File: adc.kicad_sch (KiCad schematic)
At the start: 0 parts

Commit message: First schematic version of AF
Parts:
- added U6: LTC2299xUP, Package_DFN_QFN:QFN-64-1EP_9x9mm_P0.5mm_EP7.15x7.15mm, symbol Analog_ADC:LTC2299xUP
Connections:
- new net: U6.11 (REFLB), U6.12 (REFLB)
- new net: U6.13 (REFHB), U6.14 (REFHB)
- new net: U6.17 (GND), U6.64 (GND), U6.65 (GND)
- new net: U6.3 (REFHA), U6.4 (REFHA)
- new net: U6.31 (OGND), U6.50 (OGND)
- new net: U6.5 (REFLA), U6.6 (REFLA)
- new net CH1_CH+: U6.1 (AINA+)
- new net CH1_CH-: U6.2 (AINA-)
- new net CH1_COMMON: U6.61 (VCMA)
- new net CH2_CH+: U6.16 (AINB+)
- new net CH2_CH-: U6.15 (AINB-)
- new net CH2_COMMON: U6.20 (VCMB)

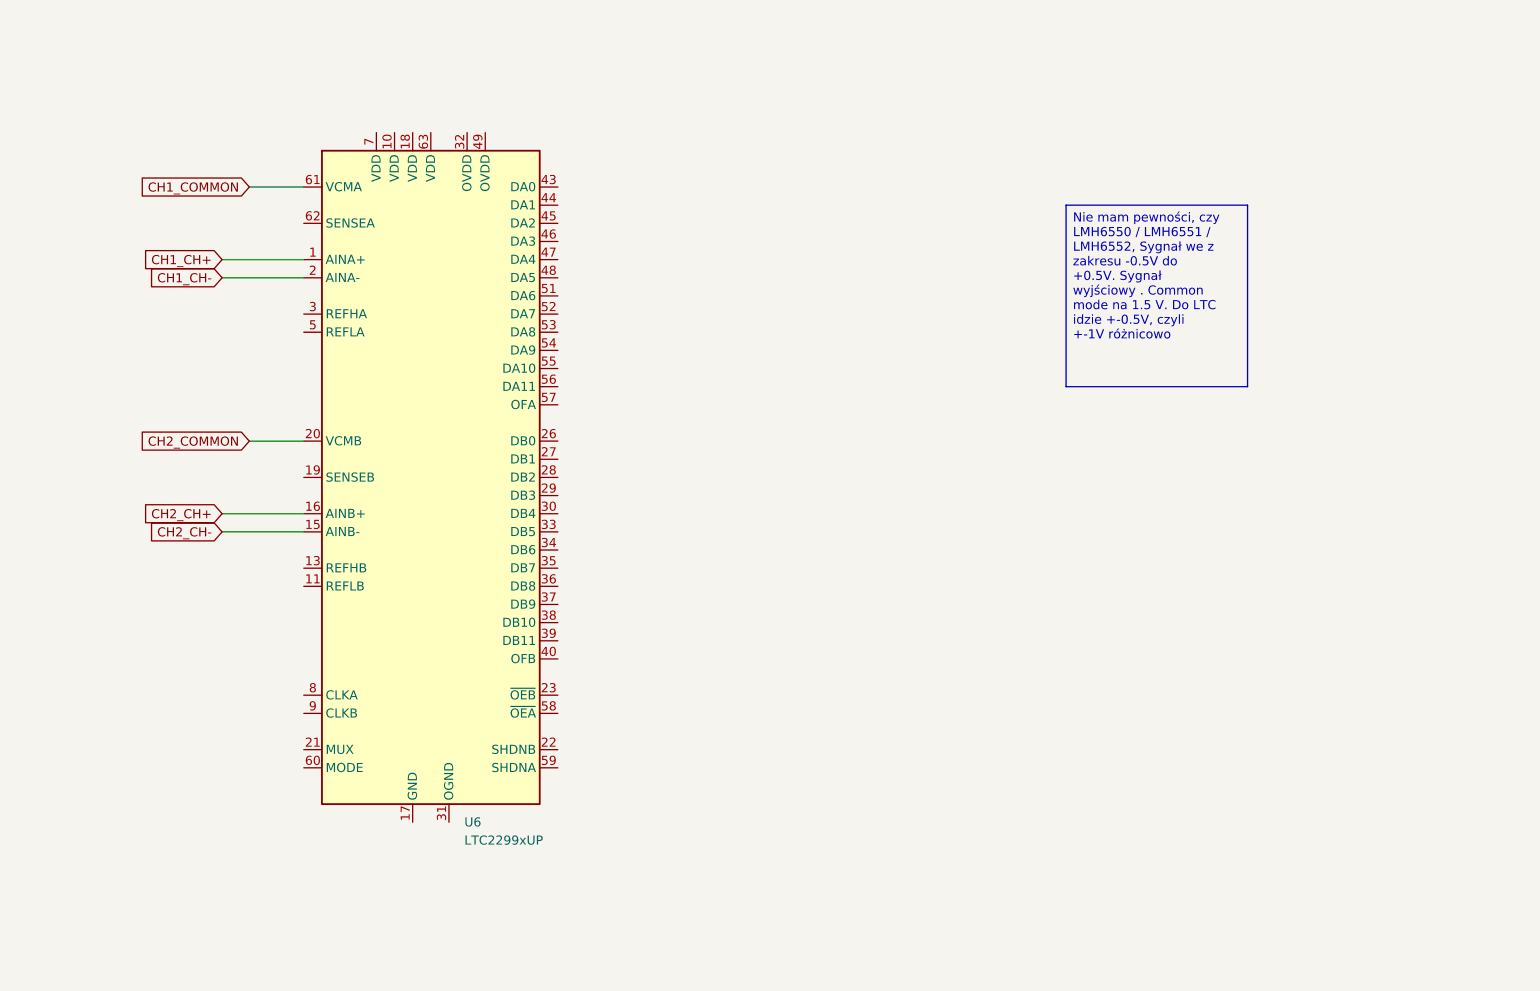
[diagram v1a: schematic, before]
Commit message: Chose amplifiers
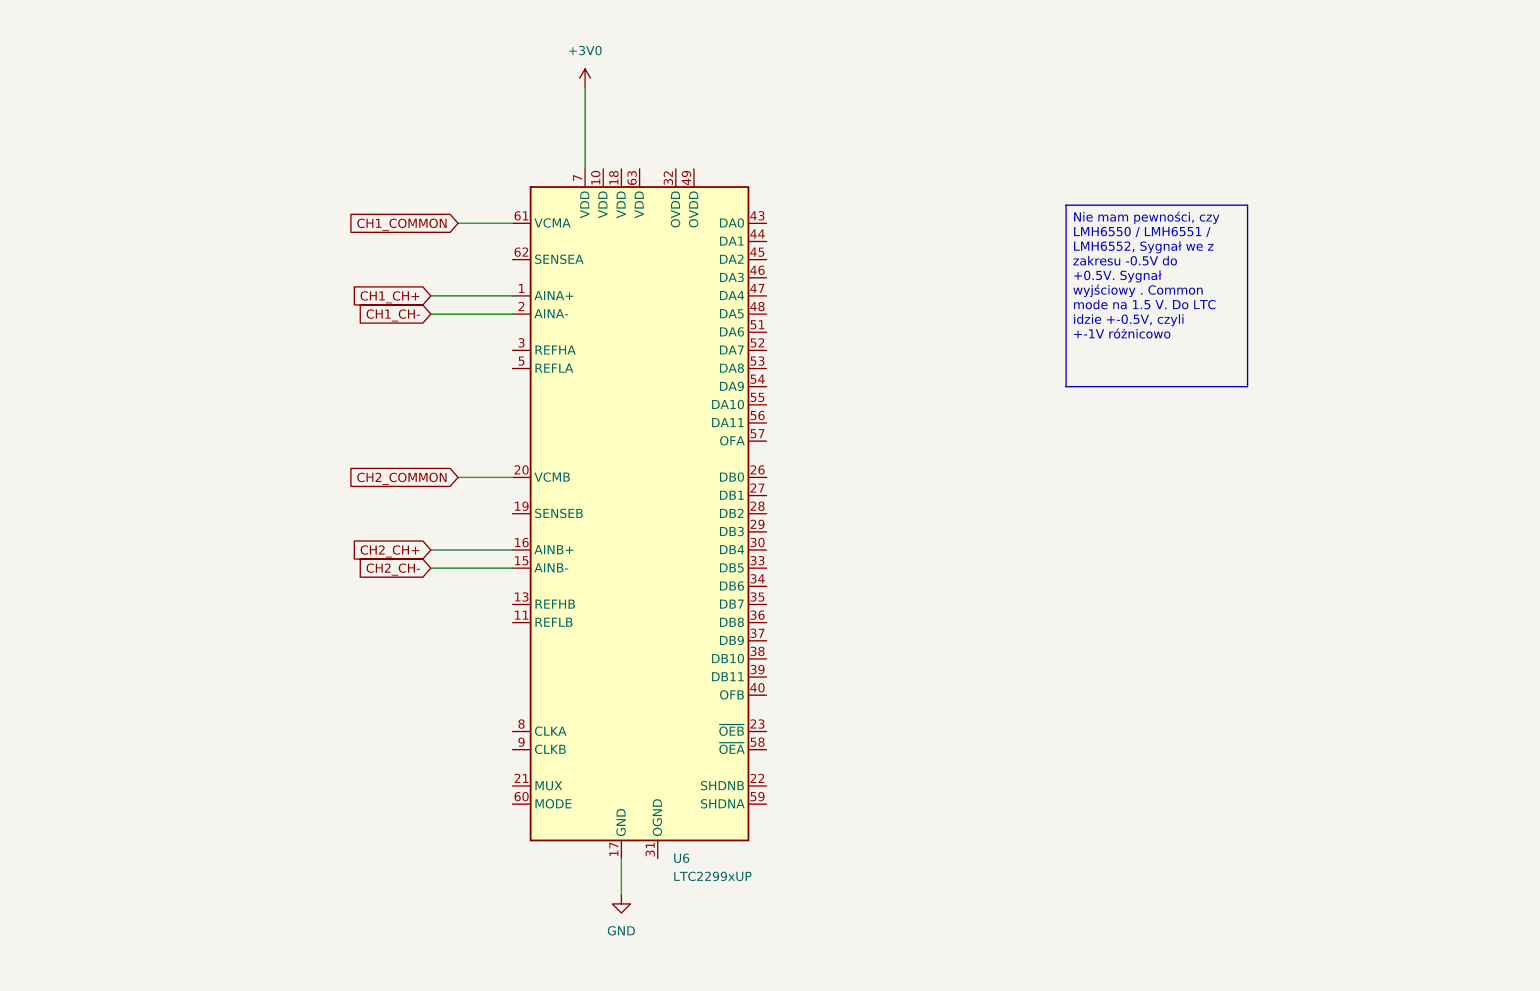
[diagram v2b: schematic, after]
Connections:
- net GND: now reaches U6.17 (GND), U6.64 (GND), U6.65 (GND)
- net +3V0: now reaches U6.7 (VDD)
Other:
- moved on the sheet: U6
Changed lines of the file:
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@@
 	(wire
 		(pts
-			(xy 92.71 91.44) (xy 104.14 91.44)
-		)
-		(stroke
-			(width 0)
-			(type default)
-		)
-	)
-	(wire
-		(pts
-			(xy 96.52 45.72) (xy 104.14 45.72)
-		)
-		(stroke
-			(width 0)
-			(type default)
-		)
-	)
-	(wire
-		(pts
-			(xy 92.71 55.88) (xy 104.14 55.88)
-		)
-		(stroke
-			(width 0)
-			(type default)
-		)
-	)
-	(wire
-		(pts
-			(xy 92.71 58.42) (xy 104.14 58.42)
-		)
-		(stroke
-			(width 0)
-			(type default)
-		)
-	)
-	(wire
-		(pts
-			(xy 96.52 81.28) (xy 104.14 81.28)
-		)
-		(stroke
-			(width 0)
-			(type default)
-		)
-	)
-	(wire
-		(pts
-			(xy 92.71 93.98) (xy 104.14 93.98)
+			(xy 143.51 31.75) (xy 143.51 43.18)
+		)
+		(stroke
+			(width 0)
+			(type default)
+		)
+	)
+	(wire
+		(pts
+			(xy 121.92 96.52) (xy 133.35 96.52)
+		)
+		(stroke
+			(width 0)
+			(type default)
+		)
+	)
+	(wire
+		(pts
+			(xy 125.73 50.8) (xy 133.35 50.8)
+		)
+		(stroke
+			(width 0)
+			(type default)
+		)
+	)
+	(wire
+		(pts
+			(xy 121.92 60.96) (xy 133.35 60.96)
+		)
+		(stroke
+			(width 0)
+			(type default)
+		)
+	)
+	(wire
+		(pts
+			(xy 121.92 63.5) (xy 133.35 63.5)
+		)
+		(stroke
+			(width 0)
+			(type default)
+		)
+	)
+	(wire
+		(pts
+			(xy 125.73 86.36) (xy 133.35 86.36)
+		)
+		(stroke
+			(width 0)
+			(type default)
+		)
+	)
+	(wire
+		(pts
+			(xy 148.59 139.7) (xy 148.59 144.78)
+		)
+		(stroke
+			(width 0)
+			(type default)
+		)
+	)
+	(wire
+		(pts
+			(xy 121.92 99.06) (xy 133.35 99.06)
 		)
 		(stroke
@@
 	(global_label "CH2_CH-"
 		(shape input)
-		(at 92.71 93.98 180)
+		(at 121.92 99.06 180)
 		(fields_autoplaced yes)
 		(effects
@@
 		)
 		(property "Intersheetrefs" "${INTERSHEET_REFS}"
-			(at 80.7743 93.98 0)
+			(at 109.9843 99.06 0)
 			(effects
 				(font
@@
 	(global_label "CH1_CH+"
 		(shape input)
-		(at 92.71 55.88 180)
+		(at 121.92 60.96 180)
 		(fields_autoplaced yes)
 		(effects
@@
 		)
 		(property "Intersheetrefs" "${INTERSHEET_REFS}"
-			(at 80.7743 55.88 0)
+			(at 109.9843 60.96 0)
 			(effects
 				(font
@@
 	(global_label "CH1_CH-"
 		(shape input)
-		(at 92.71 58.42 180)
+		(at 121.92 63.5 180)
 		(fields_autoplaced yes)
 		(effects
@@
 		)
 		(property "Intersheetrefs" "${INTERSHEET_REFS}"
-			(at 80.7743 58.42 0)
+			(at 109.9843 63.5 0)
 			(effects
 				(font
@@
 	(global_label "CH1_COMMON"
 		(shape input)
-		(at 96.52 45.72 180)
+		(at 125.73 50.8 180)
 		(fields_autoplaced yes)
 		(effects
@@
 		)
 		(property "Intersheetrefs" "${INTERSHEET_REFS}"
-			(at 80.5929 45.72 0)
+			(at 109.8029 50.8 0)
 			(effects
 				(font
@@
 	(global_label "CH2_COMMON"
 		(shape input)
-		(at 96.52 81.28 180)
+		(at 125.73 86.36 180)
 		(fields_autoplaced yes)
 		(effects
@@
 		)
 		(property "Intersheetrefs" "${INTERSHEET_REFS}"
-			(at 80.5929 81.28 0)
+			(at 109.8029 86.36 0)
 			(effects
 				(font
@@
 	(global_label "CH2_CH+"
 		(shape input)
-		(at 92.71 91.44 180)
+		(at 121.92 96.52 180)
 		(fields_autoplaced yes)
 		(effects
@@
 		)
 		(property "Intersheetrefs" "${INTERSHEET_REFS}"
-			(at 80.7743 91.44 0)
+			(at 109.9843 96.52 0)
 			(effects
 				(font
@@
 	(symbol
 		(lib_id "Analog_ADC:LTC2299xUP")
-		(at 121.92 86.36 0)
+		(at 151.13 91.44 0)
 		(unit 1)
 		(exclude_from_sim no)
@@
 		(fields_autoplaced yes)
 		(property "Reference" "U6"
-			(at 126.6033 134.62 0)
+			(at 155.8133 139.7 0)
 			(effects
 				(font
@@
 		)
 		(property "Value" "LTC2299xUP"
-			(at 126.6033 137.16 0)
+			(at 155.8133 142.24 0)
 			(effects
 				(font
@@
 		)
 		(property "Footprint" "Package_DFN_QFN:QFN-64-1EP_9x9mm_P0.5mm_EP7.15x7.15mm"
-			(at 121.92 88.9 0)
+			(at 151.13 93.98 0)
 			(effects
 				(font
@@
 		)
 		(property "Datasheet" "https://www.analog.com/media/en/technical-documentation/data-sheets/2299fa.pdf"
-			(at 121.92 86.36 0)
+			(at 151.13 91.44 0)
 			(effects
 				(font
@@
 		)
 		(property "Description" "Dual-Channel, 14-Bit Low Power ADC, 80Msps, QFN-64"
-			(at 121.92 86.36 0)
+			(at 151.13 91.44 0)
 			(effects
 				(font
@@
 					(unit 1)
 				)
+			)
+		)
+	)
+	(symbol
+		(lib_id "power:GND")
+		(at 148.59 144.78 0)
+		(unit 1)
+		(exclude_from_sim no)
+		(in_bom yes)
+		(on_board yes)
+		(dnp no)
+		(fields_autoplaced yes)
+		(property "Reference" "#PWR025"
+			(at 148.59 151.13 0)
+			(effects
+				(font
+					(size 1.27 1.27)
+				)
+				(hide yes)
+			)
+		)
+		(property "Value" "GND"
+			(at 148.59 149.86 0)
+			(effects
+				(font
+					(size 1.27 1.27)
+				)
+			)
+		)
+		(property "Footprint" ""
+			(at 148.59 144.78 0)
+			(effects
+				(font
+					(size 1.27 1.27)
+				)
+				(hide yes)
+			)
+		)
+		(property "Datasheet" ""
+			(at 148.59 144.78 0)
+			(effects
+				(font
+					(size 1.27 1.27)
+				)
+				(hide yes)
+			)
+		)
+		(property "Description" "Power symbol creates a global label with name \"GND\" , ground"
+			(at 148.59 144.78 0)
+			(effects
+				(font
+					(size 1.27 1.27)
+				)
+				(hide yes)
+			)
+		)
+		(pin "1"
+		)
+		(instances
+			(project ""
+				(path "/553deb7b-4100-40fe-99d2-0c7b4b56aad2/800cc051-5da0-4b0f-90b7-cfba3f489ea8"
+					(reference "#PWR025")
+					(unit 1)
+				)
+			)
+		)
+	)
+	(symbol
+		(lib_id "power:+3V0")
+		(at 143.51 31.75 0)
+		(unit 1)
+		(exclude_from_sim no)
+		(in_bom yes)
+		(on_board yes)
+		(dnp no)
+		(fields_autoplaced yes)
+		(property "Reference" "#PWR026"
+			(at 143.51 35.56 0)
+			(effects
+				(font
+					(size 1.27 1.27)
+				)
+				(hide yes)
+			)
+		)
+		(property "Value" "+3V0"
+			(at 143.51 26.67 0)
+			(effects
+				(font
+					(size 1.27 1.27)
+				)
+			)
+		)
+		(property "Footprint" ""
+			(at 143.51 31.75 0)
+			(effects
+				(font
+					(size 1.27 1.27)
+				)
+				(hide yes)
+			)
+		)
+		(property "Datasheet" ""
+			(at 143.51 31.75 0)
+			(effects
+				(font
+					(size 1.27 1.27)
+				)
+				(hide yes)
+			)
+		)
+		(property "Description" "Power symbol creates a global label with name \"+3V0\""
+			(at 143.51 31.75 0)
+			(effects
+				(font
+					(size 1.27 1.27)
+				)
+				(hide yes)
+			)
+		)
+		(pin "1"
+		)
+		(instances
+			(project ""
+				(path "/553deb7b-4100-40fe-99d2-0c7b4b56aad2/800cc051-5da0-4b0f-90b7-cfba3f489ea8"
+					(reference "#PWR026")
+					(unit 1)
+				)

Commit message: Add some of the AF power supply levels
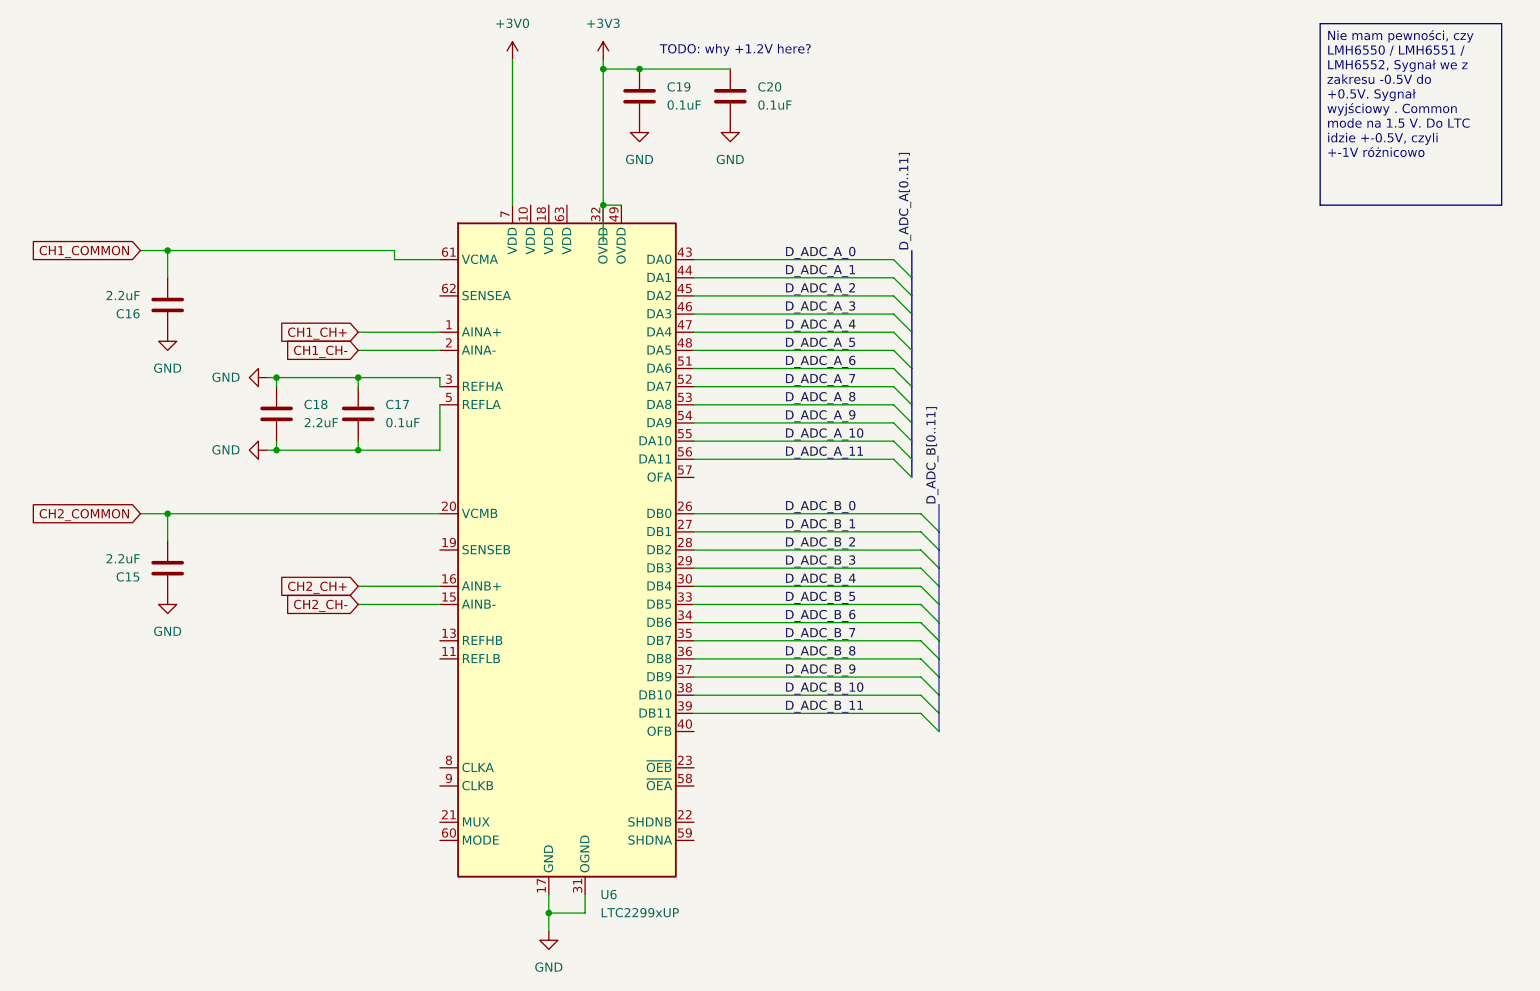
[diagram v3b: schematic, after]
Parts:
- added C15, C16, C18: 2.2uF, symbol Device:C
- added C17, C19, C20: 0.1uF, symbol Device:C
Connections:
- net CH1_COMMON: now also C16.1
- net CH2_COMMON: now also C15.1
- net GND: now also U6.3 (REFHA), U6.31 (OGND), U6.4 (REFHA), U6.5 (REFLA), U6.50 (OGND), U6.6 (REFLA), C15.2, C16.2, C17.1, C17.2, C18.1, C18.2, C19.2, C20.1
- net D_ADC_B_0: now reaches U6.26 (DB0)
- net D_ADC_B_1: now reaches U6.27 (DB1)
- net D_ADC_B_2: now reaches U6.28 (DB2)
- net D_ADC_B_3: now reaches U6.29 (DB3)
- net D_ADC_B_4: now reaches U6.30 (DB4)
- net +3V3: now reaches U6.32 (OVDD)
- net +3V3: now also U6.49 (OVDD), C19.1, C20.2
- net D_ADC_B_5: now reaches U6.33 (DB5)
- net D_ADC_B_6: now reaches U6.34 (DB6)
- net D_ADC_B_7: now reaches U6.35 (DB7)
- net D_ADC_B_8: now reaches U6.36 (DB8)
- net D_ADC_B_9: now reaches U6.37 (DB9)
- net D_ADC_B_10: now reaches U6.38 (DB10)
- net D_ADC_B_11: now reaches U6.39 (DB11)
- net D_ADC_A_0: now reaches U6.43 (DA0)
- net D_ADC_A_1: now reaches U6.44 (DA1)
- net D_ADC_A_2: now reaches U6.45 (DA2)
- net D_ADC_A_3: now reaches U6.46 (DA3)
- net D_ADC_A_4: now reaches U6.47 (DA4)
- net D_ADC_A_5: now reaches U6.48 (DA5)
- net D_ADC_A_6: now reaches U6.51 (DA6)
- net D_ADC_A_7: now reaches U6.52 (DA7)
- net D_ADC_A_8: now reaches U6.53 (DA8)
- net D_ADC_A_9: now reaches U6.54 (DA9)
- net D_ADC_A_10: now reaches U6.55 (DA10)
- net D_ADC_A_11: now reaches U6.56 (DA11)
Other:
- note added: "TODO: why +1.2V here?"
- moved on the sheet: U6
